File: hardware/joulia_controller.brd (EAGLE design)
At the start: 121 x 68 mm, 41 parts, among them IC1 LM2902D, IC2 LM2902D, U1 MMBT2222ALT1G, U2 MMBT2222ALT1G

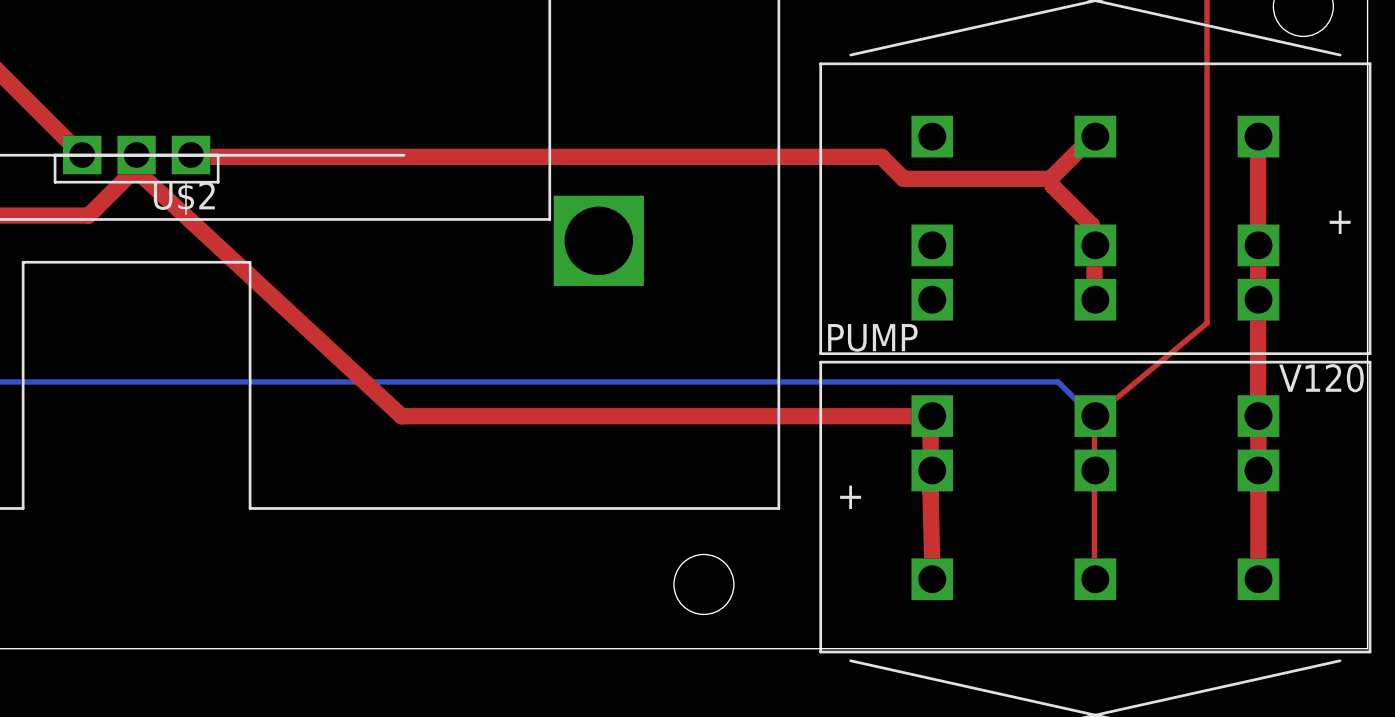
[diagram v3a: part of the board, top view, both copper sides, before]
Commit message: Rewiring pump to be consistent with HE.
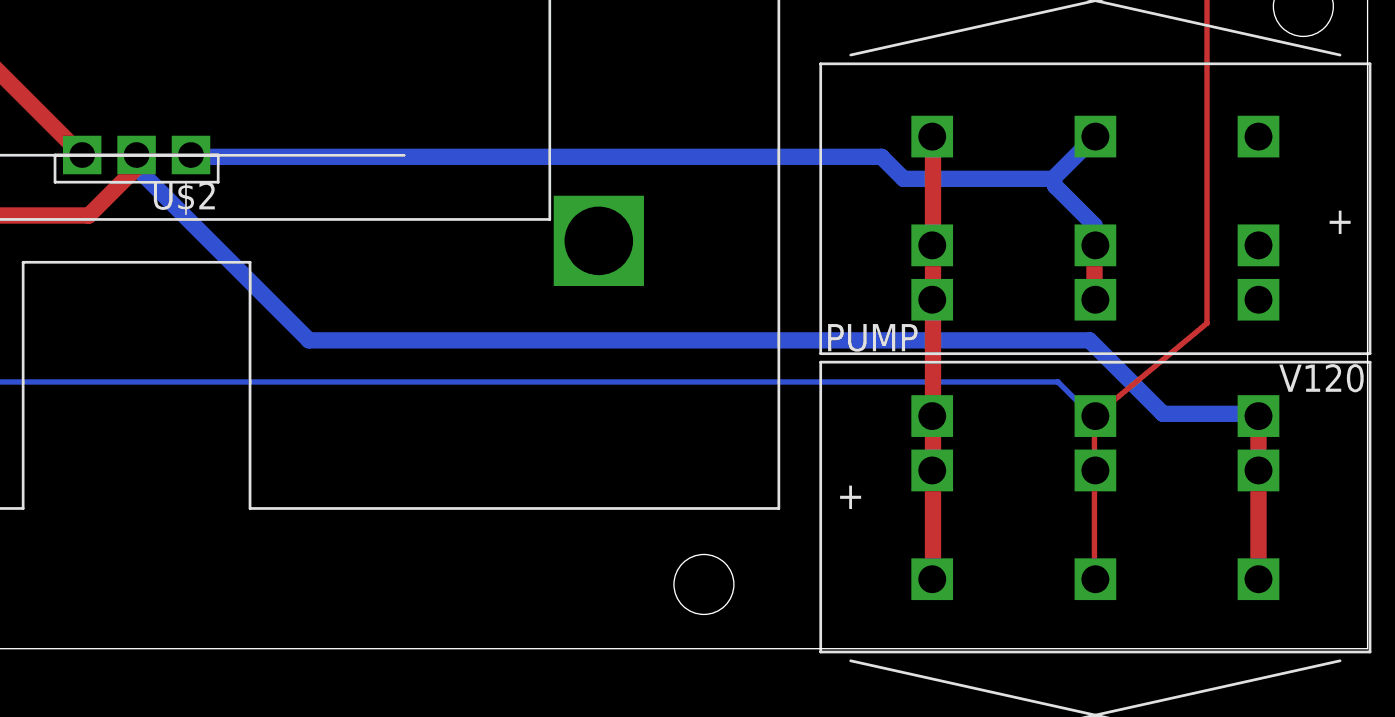
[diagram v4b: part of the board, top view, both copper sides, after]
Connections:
- net N$26 renamed 120H
- net N$29 renamed +120
- net N$32 renamed -120
- removed net N$27: PUMP.P$4, PUMP.P$5, PUMP.P$6, V120.P$7, V120.P$8, V120.P$9
- new net 120N: PUMP.P$7, PUMP.P$8, PUMP.P$9, V120.P$4, V120.P$5, V120.P$6
- net N$24: now also PUMP.P$4, PUMP.P$5, PUMP.P$6; no longer PUMP.P$7, PUMP.P$8, PUMP.P$9
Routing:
- net N$27: track 23.1 -> 0.00 mm
- net 120N: track 0.00 -> 20.8 mm
- net N$24: track 69.9 -> 84.3 mm
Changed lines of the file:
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@@
 <contactref element="U$2" pad="A2"/>
 <wire x1="47.5488" y1="23.0124" x2="47.495" y2="23.08" width="0.254" layer="1"/>
-<contactref element="PUMP" pad="P$8"/>
-<contactref element="PUMP" pad="P$7"/>
-<contactref element="PUMP" pad="P$9"/>
-<wire x1="100.584" y1="7.3152" x2="100.684" y2="3.2003" width="0.762" layer="1"/>
-<wire x1="100.684" y1="3.2003" x2="100.665" y2="3.245" width="0.762" layer="1"/>
-<wire x1="100.584" y1="7.3152" x2="100.665" y2="8.325" width="0.762" layer="1"/>
-<wire x1="100.584" y1="7.7724" x2="100.584" y2="9.9441" width="0.762" layer="1"/>
-<wire x1="100.584" y1="9.9441" x2="100.665" y2="10.865" width="0.762" layer="1"/>
-<wire x1="100.584" y1="7.7724" x2="100.665" y2="8.325" width="0.762" layer="1"/>
 <wire x1="63.4365" y1="22.4028" x2="63.4365" y2="22.9743" width="0.762" layer="1"/>
 <wire x1="61.2648" y1="20.2311" x2="63.4365" y2="22.4028" width="0.762" layer="1"/>
@@
 <wire x1="63.4365" y1="22.9743" x2="63.5" y2="23.06" width="0.762" layer="1"/>
 <wire x1="47.6631" y1="22.9743" x2="47.495" y2="23.08" width="0.762" layer="1"/>
-<wire x1="75.8809" y1="10.8584" x2="100.6411" y2="10.8584" width="0.762" layer="1"/>
-<wire x1="63.6651" y1="22.1742" x2="75.8809" y2="10.8584" width="0.762" layer="1"/>
-<wire x1="100.6411" y1="10.8584" x2="100.665" y2="10.865" width="0.762" layer="1"/>
-<wire x1="63.6651" y1="22.1742" x2="63.5" y2="23.06" width="0.762" layer="1"/>
+<contactref element="PUMP" pad="P$5"/>
+<contactref element="PUMP" pad="P$6"/>
+<contactref element="PUMP" pad="P$4"/>
+<wire x1="115.9002" y1="8.2296" x2="115.9002" y2="3.3147" width="0.762" layer="1"/>
+<wire x1="115.9002" y1="3.3147" x2="115.905" y2="3.245" width="0.762" layer="1"/>
+<wire x1="115.9002" y1="8.2296" x2="115.905" y2="8.325" width="0.762" layer="1"/>
+<wire x1="115.9002" y1="8.6868" x2="115.9002" y2="10.8585" width="0.762" layer="1"/>
+<wire x1="115.9002" y1="10.8585" x2="115.905" y2="10.865" width="0.762" layer="1"/>
+<wire x1="115.9002" y1="8.6868" x2="115.905" y2="8.325" width="0.762" layer="1"/>
+<wire x1="111.4425" y1="10.9728" x2="115.9002" y2="10.9728" width="0.762" layer="16"/>
+<wire x1="108.0135" y1="14.4018" x2="111.4425" y2="10.9728" width="0.762" layer="16"/>
+<wire x1="71.5518" y1="14.4018" x2="108.0135" y2="14.4018" width="0.762" layer="16"/>
+<wire x1="63.5508" y1="22.4028" x2="71.5518" y2="14.4018" width="0.762" layer="16"/>
+<wire x1="63.5508" y1="22.9743" x2="63.5508" y2="22.4028" width="0.762" layer="16"/>
+<wire x1="115.9002" y1="10.9728" x2="115.905" y2="10.865" width="0.762" layer="16"/>
+<wire x1="63.5508" y1="22.9743" x2="63.5" y2="23.06" width="0.762" layer="16"/>
 </signal>
-<signal name="N$26" class="1">
+<signal name="120H" class="1">
 <contactref element="U$2" pad="A1"/>
 <contactref element="V120" pad="P$3"/>
@@
 <wire x1="108.2421" y1="16.3449" x2="108.285" y2="16.3" width="0.762" layer="1"/>
 <wire x1="108.2421" y1="18.7452" x2="108.285" y2="18.84" width="0.762" layer="1"/>
-<wire x1="98.298" y1="22.9743" x2="66.0654" y2="22.9743" width="0.762" layer="1"/>
-<wire x1="99.3267" y1="21.9456" x2="98.298" y2="22.9743" width="0.762" layer="1"/>
-<wire x1="106.1847" y1="21.9456" x2="99.3267" y2="21.9456" width="0.762" layer="1"/>
-<wire x1="108.1278" y1="23.8887" x2="106.1847" y2="21.9456" width="0.762" layer="1"/>
-<wire x1="66.0654" y1="22.9743" x2="66.04" y2="23.06" width="0.762" layer="1"/>
-<wire x1="108.1278" y1="23.8887" x2="108.285" y2="23.92" width="0.762" layer="1"/>
-<wire x1="108.1278" y1="19.7739" x2="108.1278" y2="19.2024" width="0.762" layer="1"/>
-<wire x1="106.299" y1="21.6027" x2="108.1278" y2="19.7739" width="0.762" layer="1"/>
-<wire x1="108.1278" y1="19.2024" x2="108.285" y2="18.84" width="0.762" layer="1"/>
-<wire x1="106.299" y1="21.6027" x2="106.1847" y2="21.9456" width="0.762" layer="1"/>
+<wire x1="98.298" y1="22.9743" x2="66.0654" y2="22.9743" width="0.762" layer="16"/>
+<wire x1="99.3267" y1="21.9456" x2="98.298" y2="22.9743" width="0.762" layer="16"/>
+<wire x1="106.299" y1="21.9456" x2="99.3267" y2="21.9456" width="0.762" layer="16"/>
+<wire x1="108.2421" y1="23.8887" x2="106.299" y2="21.9456" width="0.762" layer="16"/>
+<wire x1="66.0654" y1="22.9743" x2="66.04" y2="23.06" width="0.762" layer="16"/>
+<wire x1="108.2421" y1="23.8887" x2="108.285" y2="23.92" width="0.762" layer="16"/>
+<wire x1="108.2421" y1="19.7739" x2="108.2421" y2="18.8595" width="0.762" layer="16"/>
+<wire x1="106.4133" y1="21.6027" x2="108.2421" y2="19.7739" width="0.762" layer="16"/>
+<wire x1="108.2421" y1="18.8595" x2="108.285" y2="18.84" width="0.762" layer="16"/>
+<wire x1="106.4133" y1="21.6027" x2="106.299" y2="21.9456" width="0.762" layer="16"/>
 </signal>
 <signal name="N$28">
@@
 <via x="23.3172" y="32.1183" extent="1-16" drill="0.6096"/>
 </signal>
-<signal name="N$32" class="2">
+<signal name="-120" class="2">
 <contactref element="V240" pad="P$3"/>
 <contactref element="V240" pad="P$1"/>
@@
 <wire x1="108.285" y1="52.2" x2="108.285" y2="44.58" width="7.62" layer="16"/>
 </signal>
-<signal name="N$27" class="1">
-<contactref element="PUMP" pad="P$4"/>
-<contactref element="PUMP" pad="P$6"/>
-<contactref element="PUMP" pad="P$5"/>
-<contactref element="V120" pad="P$7"/>
-<contactref element="V120" pad="P$9"/>
-<contactref element="V120" pad="P$8"/>
-<wire x1="115.8859" y1="18.7452" x2="115.8859" y2="16.3449" width="0.762" layer="1"/>
-<wire x1="115.8859" y1="16.3449" x2="115.905" y2="16.3" width="0.762" layer="1"/>
-<wire x1="115.8859" y1="18.7452" x2="115.905" y2="18.84" width="0.762" layer="1"/>
-<wire x1="115.8859" y1="19.2024" x2="115.8859" y2="23.8887" width="0.762" layer="1"/>
-<wire x1="115.8859" y1="23.8887" x2="115.905" y2="23.92" width="0.762" layer="1"/>
-<wire x1="115.8859" y1="19.2024" x2="115.905" y2="18.84" width="0.762" layer="1"/>
-<wire x1="115.9002" y1="7.3152" x2="115.9002" y2="3.2003" width="0.762" layer="1"/>
-<wire x1="115.9002" y1="3.2003" x2="115.905" y2="3.245" width="0.762" layer="1"/>
-<wire x1="115.9002" y1="7.3152" x2="115.905" y2="8.325" width="0.762" layer="1"/>
-<wire x1="115.9002" y1="7.7724" x2="115.9002" y2="9.9441" width="0.762" layer="1"/>
-<wire x1="115.9002" y1="9.9441" x2="115.905" y2="10.865" width="0.762" layer="1"/>
-<wire x1="115.9002" y1="7.7724" x2="115.905" y2="8.325" width="0.762" layer="1"/>
-<wire x1="115.8859" y1="10.287" x2="115.8859" y2="16.302" width="0.762" layer="1"/>
-<wire x1="115.8859" y1="16.302" x2="115.905" y2="16.3" width="0.762" layer="1"/>
-<wire x1="115.8859" y1="10.287" x2="115.905" y2="10.865" width="0.762" layer="1"/>
-</signal>
-<signal name="N$29" class="2">
+<signal name="+120" class="2">
 <contactref element="HEAT" pad="P$8"/>
 <contactref element="HEAT" pad="P$7"/>
@@
 <wire x1="115.905" y1="60.175" x2="115.905" y2="65.255" width="0.762" layer="16"/>
 </signal>
+<signal name="120N" class="1">
+<contactref element="PUMP" pad="P$8"/>
+<contactref element="PUMP" pad="P$7"/>
+<contactref element="PUMP" pad="P$9"/>
+<contactref element="V120" pad="P$5"/>
+<contactref element="V120" pad="P$6"/>
+<contactref element="V120" pad="P$4"/>
+<wire x1="100.6983" y1="8.2296" x2="100.6983" y2="3.3147" width="0.762" layer="1"/>
+<wire x1="100.6983" y1="3.3147" x2="100.665" y2="3.245" width="0.762" layer="1"/>
+<wire x1="100.6983" y1="8.2296" x2="100.665" y2="8.325" width="0.762" layer="1"/>
+<wire x1="100.6983" y1="8.6868" x2="100.6983" y2="10.8585" width="0.762" layer="1"/>
+<wire x1="100.6983" y1="10.8585" x2="100.665" y2="10.865" width="0.762" layer="1"/>
+<wire x1="100.6983" y1="8.6868" x2="100.665" y2="8.325" width="0.762" layer="1"/>
+<wire x1="100.6983" y1="18.7452" x2="100.6983" y2="16.3449" width="0.762" layer="1"/>
+<wire x1="100.6983" y1="16.3449" x2="100.665" y2="16.3" width="0.762" layer="1"/>
+<wire x1="100.6983" y1="18.7452" x2="100.665" y2="18.84" width="0.762" layer="1"/>
+<wire x1="100.6983" y1="19.2024" x2="100.6983" y2="23.8887" width="0.762" layer="1"/>
+<wire x1="100.6983" y1="23.8887" x2="100.665" y2="23.92" width="0.762" layer="1"/>
+<wire x1="100.6983" y1="19.2024" x2="100.665" y2="18.84" width="0.762" layer="1"/>
+<wire x1="100.6983" y1="16.002" x2="100.6983" y2="11.2014" width="0.762" layer="1"/>
+<wire x1="100.6983" y1="11.2014" x2="100.665" y2="10.865" width="0.762" layer="1"/>
+<wire x1="100.6983" y1="16.002" x2="100.665" y2="16.3" width="0.762" layer="1"/>
+</signal>
 </signals>
